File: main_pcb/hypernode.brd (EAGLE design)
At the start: 92.5 x 100 mm, 31 parts, among them IC1 74HCT245D, U1 MAX488, X2 JST-XH-CONNECTOR-02-PIN, X4 JST-XH-CONNECTOR-02-PIN, X7 JST-XH-03-PIN-LONG-PAD, X8 JST-XH-03-PIN-LONG-PAD

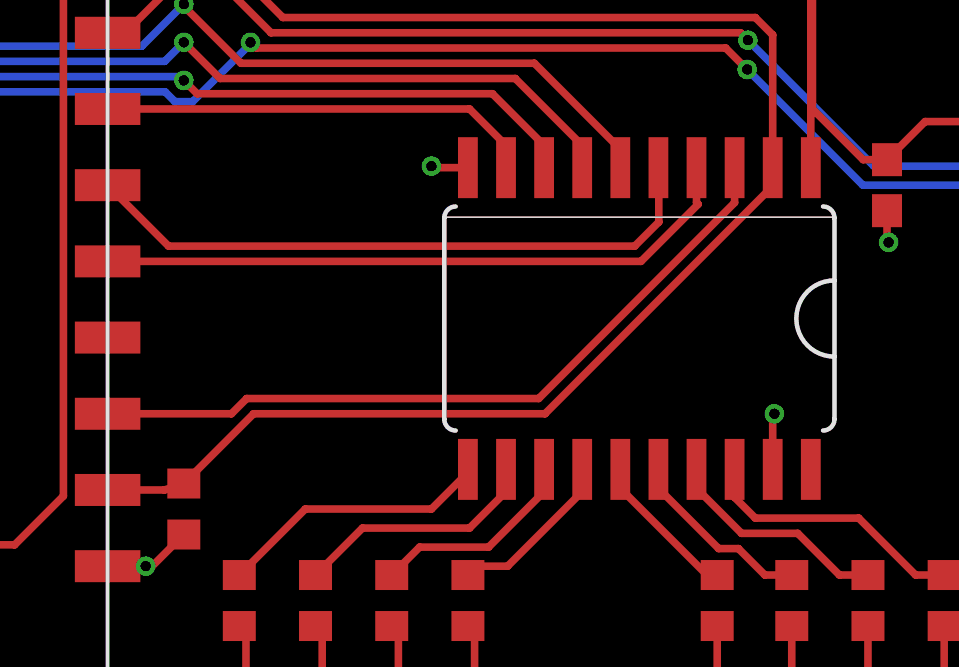
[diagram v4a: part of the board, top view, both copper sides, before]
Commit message: copy fornt panel from hyperion
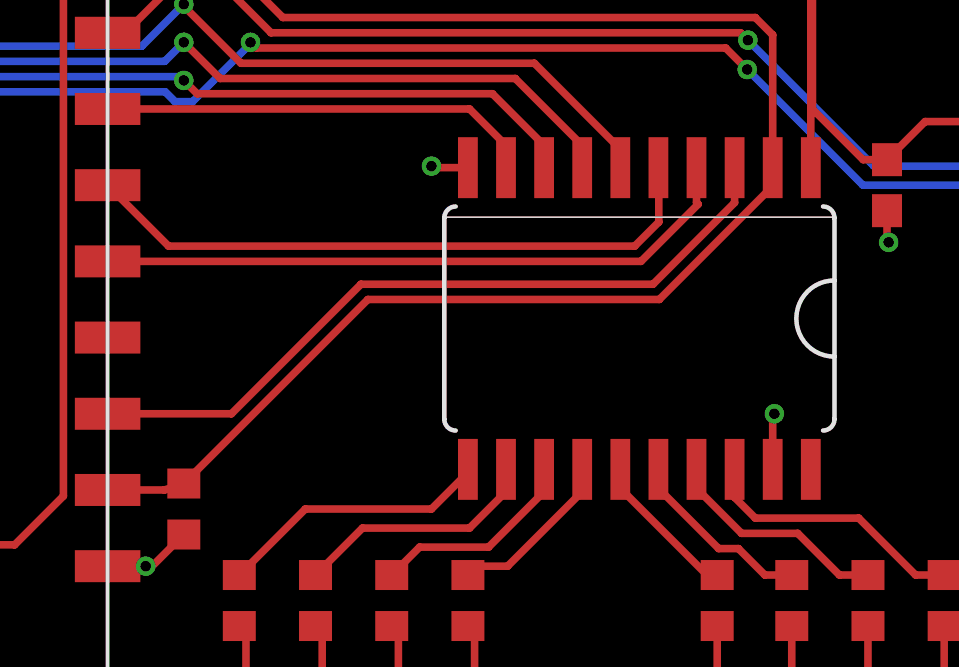
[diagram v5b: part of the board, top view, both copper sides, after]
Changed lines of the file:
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@@
 <layer number="25" name="tNames" color="7" fill="1" visible="yes" active="yes"/>
 <layer number="26" name="bNames" color="7" fill="1" visible="yes" active="yes"/>
-<layer number="27" name="tValues" color="7" fill="1" visible="no" active="yes"/>
-<layer number="28" name="bValues" color="7" fill="1" visible="no" active="yes"/>
+<layer number="27" name="tValues" color="7" fill="1" visible="yes" active="yes"/>
+<layer number="28" name="bValues" color="7" fill="1" visible="yes" active="yes"/>
 <layer number="29" name="tStop" color="7" fill="3" visible="no" active="yes"/>
 <layer number="30" name="bStop" color="7" fill="6" visible="no" active="yes"/>
@@
 <layer number="113" name="IDFDebug" color="7" fill="1" visible="no" active="yes"/>
 <layer number="116" name="Patch_BOT" color="7" fill="1" visible="no" active="yes"/>
-<layer number="121" name="_tsilk" color="7" fill="1" visible="no" active="yes"/>
-<layer number="122" name="_bsilk" color="7" fill="1" visible="no" active="yes"/>
+<layer number="121" name="_tsilk" color="7" fill="1" visible="yes" active="yes"/>
+<layer number="122" name="_bsilk" color="7" fill="1" visible="yes" active="yes"/>
 <layer number="123" name="tTestmark" color="7" fill="1" visible="no" active="yes"/>
 <layer number="124" name="bTestmark" color="7" fill="1" visible="no" active="yes"/>
@@
 <wire x1="18.0975" y1="45.085" x2="16.51" y2="45.085" width="0.254" layer="1"/>
 <via x="19.05" y="44.1325" extent="1-16" drill="0.35"/>
-<wire x1="16.51" y1="45.085" x2="16.8275" y2="45.085" width="0" layer="19" extent="1-16"/>
 <via x="19.05" y="47.3075" extent="1-16" drill="0.35"/>
 <wire x1="19.05" y1="44.1325" x2="18.89125" y2="44.29125" width="0.254" layer="1"/>
@@
 <contactref element="IC1" pad="20"/>
 <contactref element="R51" pad="2"/>
-<wire x1="50.17" y1="58.84" x2="49.75" y2="58.42" width="0" layer="19" extent="1-16"/>
 <contactref element="X4" pad="1"/>
 <wire x1="55.825" y1="53.915" x2="50.145" y2="53.915" width="1.27" layer="1"/>
@@
 <contactref element="U$17" pad="P_IO4"/>
 <wire x1="62.81" y1="30.4292" x2="62.81" y2="29.2626125" width="0.254" layer="1"/>
-<wire x1="46.5455" y1="22.733" x2="46.0375" y2="22.225" width="0.254" layer="1"/>
+<wire x1="50.3555" y1="26.543" x2="46.0375" y2="22.225" width="0.254" layer="1"/>
 <wire x1="46.0375" y1="22.225" x2="41.91" y2="22.225" width="0.254" layer="1"/>
-<wire x1="62.81" y1="29.2626125" x2="56.2803875" y2="22.733" width="0.254" layer="1"/>
-<wire x1="56.2803875" y1="22.733" x2="46.5455" y2="22.733" width="0.254" layer="1"/>
+<wire x1="62.81" y1="29.2626125" x2="60.0903875" y2="26.543" width="0.254" layer="1"/>
+<wire x1="60.0903875" y1="26.543" x2="50.3555" y2="26.543" width="0.254" layer="1"/>
 </signal>
 <signal name="WS4">
@@
 <wire x1="64.08" y1="30.4292" x2="64.1562" y2="30.353" width="0.254" layer="1"/>
 <wire x1="64.1562" y1="30.353" x2="64.1562" y2="29.8903875" width="0.254" layer="1"/>
-<wire x1="64.1562" y1="29.8903875" x2="56.4908125" y2="22.225" width="0.254" layer="1"/>
-<wire x1="46.775" y1="22.225" x2="44.45" y2="19.9" width="0.254" layer="1"/>
-<wire x1="56.4908125" y1="22.225" x2="46.775" y2="22.225" width="0.254" layer="1"/>
+<wire x1="64.1562" y1="29.8903875" x2="60.3008125" y2="26.035" width="0.254" layer="1"/>
+<wire x1="50.585" y1="26.035" x2="44.45" y2="19.9" width="0.254" layer="1"/>
+<wire x1="60.3008125" y1="26.035" x2="50.585" y2="26.035" width="0.254" layer="1"/>
 <contactref element="PROGRAM" pad="5"/>
 <wire x1="10.795" y1="50.8" x2="12.7" y2="48.895" width="0.254" layer="16"/>
@@
 <wire x1="12.7" y1="46.99" x2="13.335" y2="46.355" width="0.254" layer="16"/>
 <wire x1="13.335" y1="46.355" x2="43.18" y2="46.355" width="0.254" layer="16"/>
-<wire x1="10.795" y1="50.63845" x2="10.795" y2="50.8" width="0" layer="19" extent="1-16"/>
 <wire x1="43.18" y1="46.355" x2="44.45" y2="47.625" width="0.254" layer="16"/>
 <via x="44.45" y="47.625" extent="1-16" drill="0.35"/>
@@
 <contactref element="IC1" pad="17"/>
 <contactref element="R20" pad="1"/>
-<wire x1="61.6107875" y1="20.32" x2="61.595" y2="20.32" width="0" layer="19" extent="1-16"/>
 <wire x1="61.595" y1="20.32" x2="61.5442" y2="20.3708" width="0.254" layer="1"/>
 <wire x1="61.5442" y1="20.3708" x2="61.54" y2="20.3708" width="0.254" layer="1"/>
@@
 <contactref element="IC1" pad="16"/>
 <contactref element="R16" pad="1"/>
-<wire x1="60.3407875" y1="20.32" x2="60.325" y2="20.32" width="0" layer="19" extent="1-16"/>
-<wire x1="60.2742" y1="20.3708" x2="60.27" y2="20.375" width="0" layer="19" extent="1-16"/>
 <wire x1="62.9378125" y1="17.731" x2="62.279" y2="17.731" width="0.254" layer="1"/>
 <wire x1="64.715" y1="16.85" x2="63.8188125" y2="16.85" width="0.254" layer="1"/>
@@
 <wire x1="60.27" y1="19.74" x2="60.27" y2="20.3708" width="0.254" layer="1"/>
 <wire x1="62.279" y1="17.731" x2="60.27" y2="19.74" width="0.254" layer="1"/>
-<wire x1="60.2742" y1="20.3708" x2="60.325" y2="20.32" width="0" layer="19" extent="1-16"/>
 <wire x1="60.27" y1="20.3708" x2="60.2742" y2="20.3708" width="0.254" layer="1"/>
 </signal>
@@
 <wire x1="15.24" y1="48.26" x2="15.875" y2="47.625" width="0.254" layer="1"/>
 <wire x1="15.875" y1="47.625" x2="16.51" y2="47.625" width="0.254" layer="1"/>
-<wire x1="16.51" y1="40.005" x2="16.51" y2="47.625" width="0" layer="19" extent="1-1"/>
 </signal>
 <signal name="N$3">

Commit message: measurements before origin move
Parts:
- moved LED_STATUS 3.18 mm to (11.4, 0.00), turned to 270 degrees
- moved R6 3.18 mm to (11.4, 1.91), turned to 0 degrees
- turned LED_PWR to 270 degrees
- turned R51 to 0 degrees
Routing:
- net RX: track 69.7 -> 71.2 mm
- net +5V: track 151.2 -> 150.5 mm

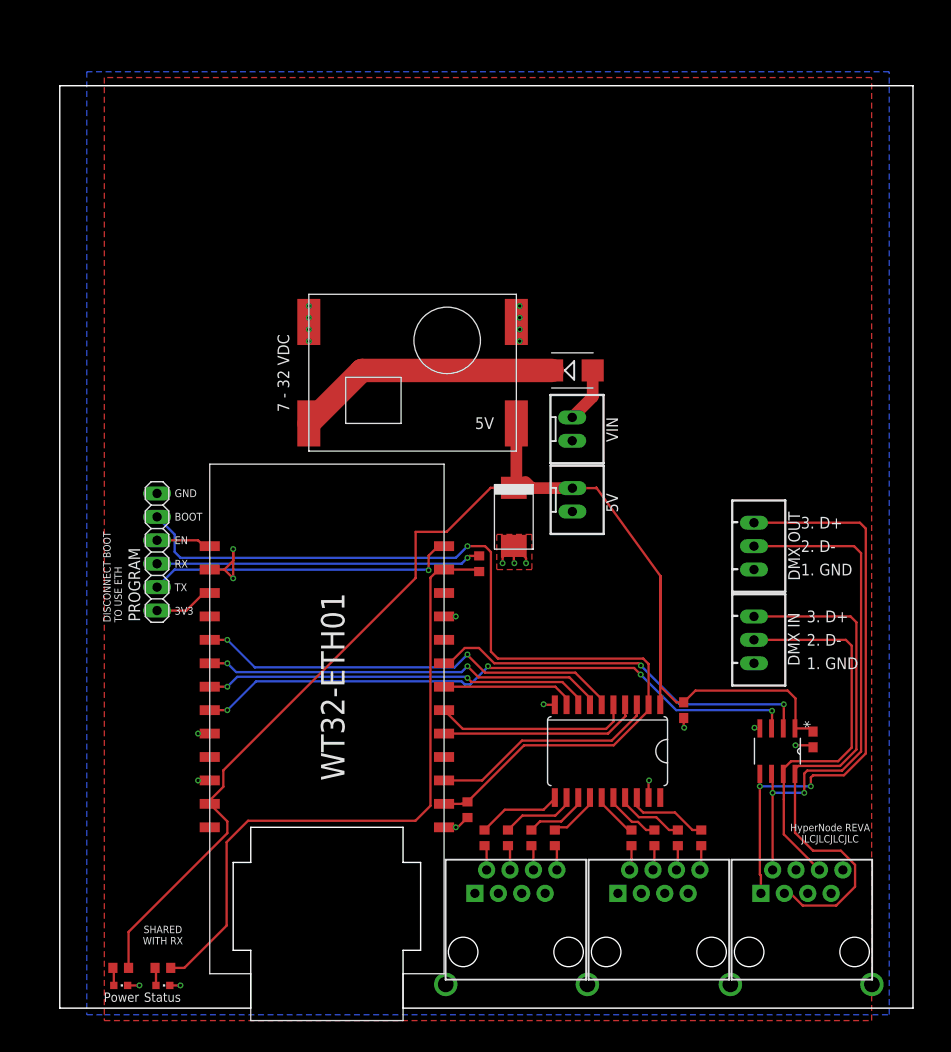
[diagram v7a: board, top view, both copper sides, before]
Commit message: move origin
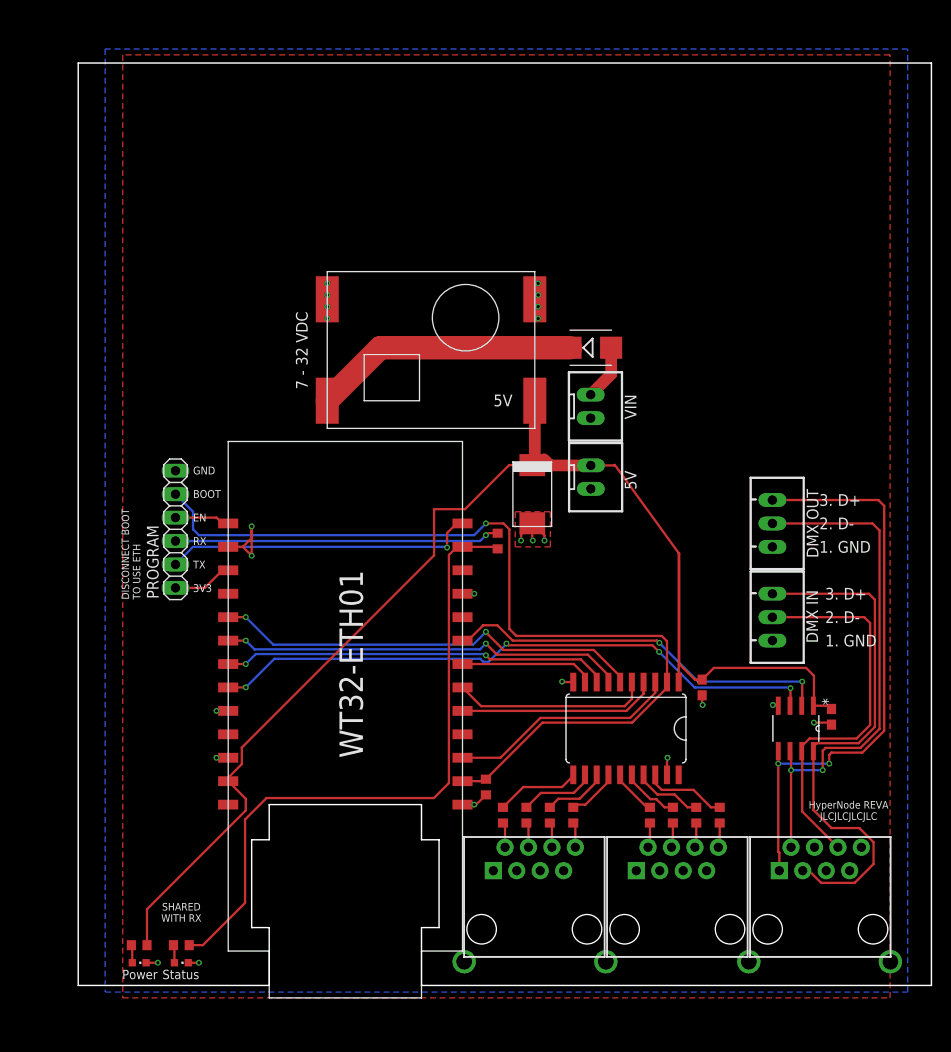
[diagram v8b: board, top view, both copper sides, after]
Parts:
- moved D2 3.17 mm to (57.8, 69.1)
- moved R3 3.17 mm to (64.2, 18.5)
- moved C1 3.17 mm to (51.5, 53.3)
- moved C5 3.17 mm to (69.9, 32.3)
- moved IC1 3.17 mm to (61.6, 27.9)
- moved PROGRAM 3.17 mm to (12.8, 49.5)
- moved R1 3.17 mm to (48.3, 18.5)
- moved R11 3.17 mm to (55.9, 18.5)
- moved R16 3.17 mm to (66.7, 18.5)
- moved R17 3.17 mm to (71.8, 18.5)
- moved R2 3.17 mm to (50.8, 18.5)
- moved R20 3.17 mm to (69.3, 18.5)
- moved R4 3.17 mm to (53.4, 18.5)
- moved R5 3.17 mm to (47.7, 48.2)
- moved R7 3.17 mm to (46.5, 21.5)
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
